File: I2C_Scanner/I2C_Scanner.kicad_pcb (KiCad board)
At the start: 4 copper layers, 63 x 30 mm, 59 parts, among them J1 USB_B_Micro, J2 Conn_01x02_Pin, J5 Conn_01x20_Pin, SW1 SW_Push, U1 RP2040, U2 NCP1117-3.3_SOT223, U3 W25Q128JVS, U4 NCP1117-1.8_SOT223, U5 TXS0108EPW, U6 TXS0108EPW, U7 TXS0108EPW, Y1 ABM8-272-T3

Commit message: v0.2
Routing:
- net +3.3V: track 32.7 -> 49.9 mm, vias 3 -> 5

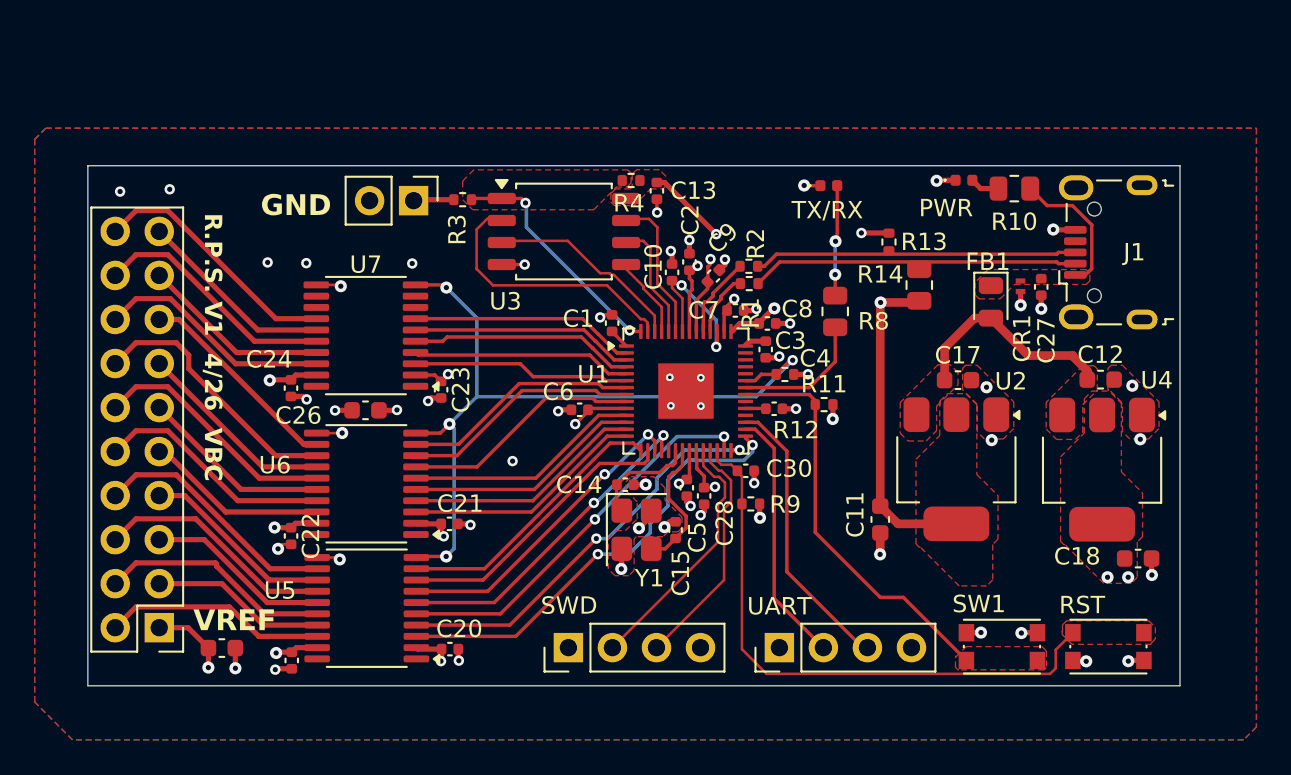
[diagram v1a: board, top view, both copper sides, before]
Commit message: Added USB C
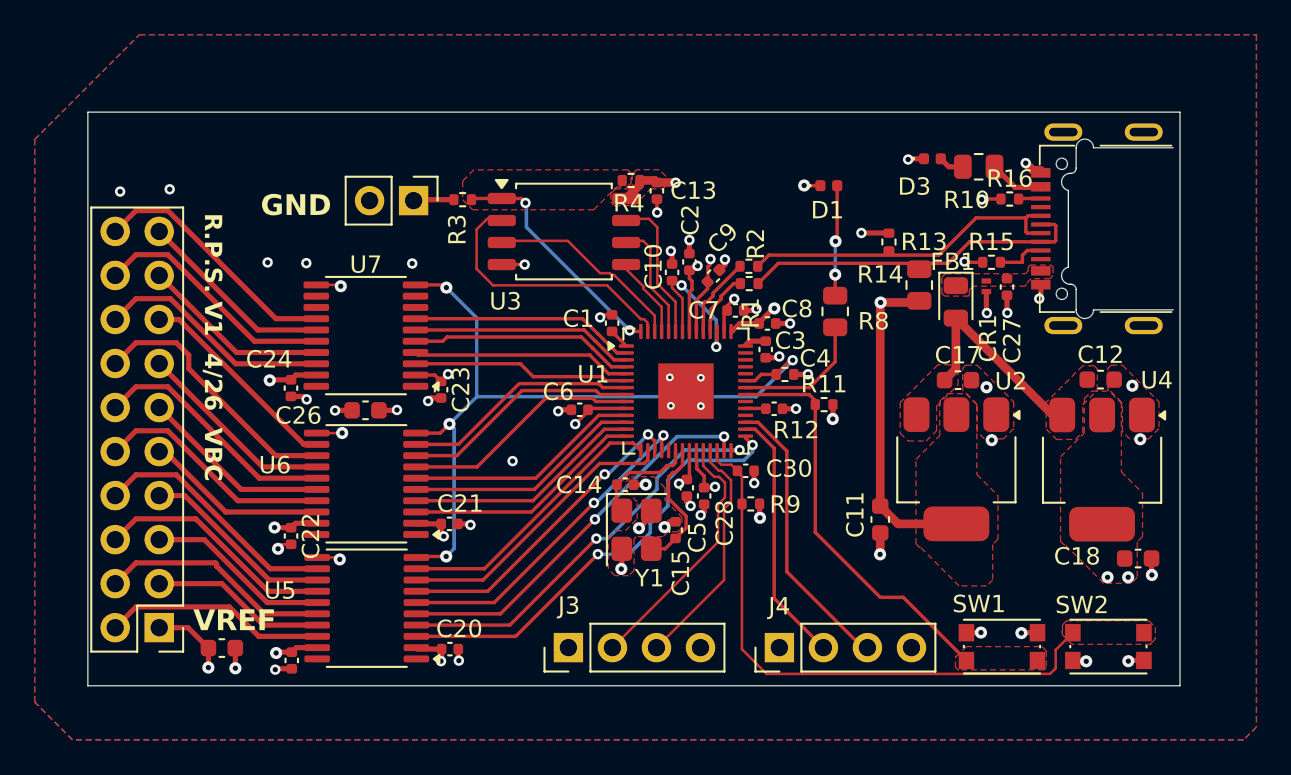
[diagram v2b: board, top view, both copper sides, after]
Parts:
- removed J1: USB_B_Micro, Connector_USB:USB_Micro-B_Wuerth_629105150521
- added J6: USB_C_Receptacle_USB2.0_14P, USB_C_Footprint:TYPE-C-31-M-14, F.Cu at (101.9, 45.6)
- added R15: 1.5KΩ, Resistor_SMD:R_0402_1005Metric, F.Cu at (94.1, 47.6)
- added R16: 1.5KΩ, Resistor_SMD:R_0402_1005Metric, F.Cu at (95.2, 43.9)
- moved R10 2.41 mm to (93.4, 42.1)
- moved D3 2.20 mm to (90.7, 41.6)
- moved FB1 2.02 mm to (92.1, 49.9)
- moved C27 1.98 mm to (95.0, 49.0)
- moved CR1 1.97 mm to (93.8, 49.0)
- renumbered TX/RX to D1, PWR to D3, SWD to J3, UART to J4, RST to SW2
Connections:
- C13 pad 1: +3.3V -> +1.8V
- R4 pad 2: +3.3V -> +1.8V
- U3 pad 8: +3.3V -> +1.8V
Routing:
- net +3.3V: track 49.9 -> 43.6 mm, vias 5 -> 4
- net /VBUS: track 8.05 -> 3.20 mm
- net +1.8V: track 24.8 -> 28.3 mm, vias 12 -> 13
- net GND: track 38.1 -> 41.5 mm, vias 55 -> 58
- net Net-(J6-CC1): track 0.00 -> 2.85 mm
- net Net-(J6-CC2): track 0.00 -> 1.29 mm
- net /USB_D-: track 18.9 -> 19.9 mm
- net /USB_D+: track 18.7 -> 19.2 mm
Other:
- board size 63 x 30 mm -> 63 x 33.1 mm

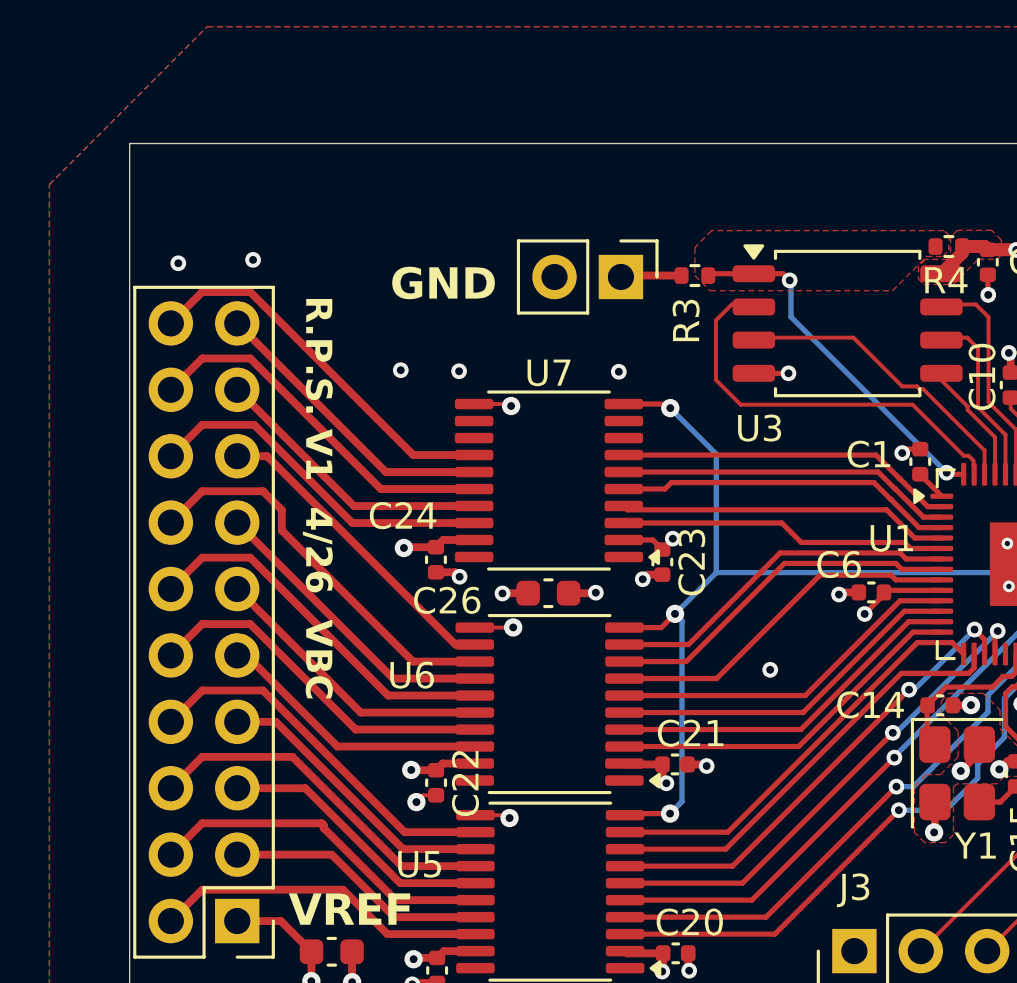
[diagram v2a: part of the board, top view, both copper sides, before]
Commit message: Added Contributer Name
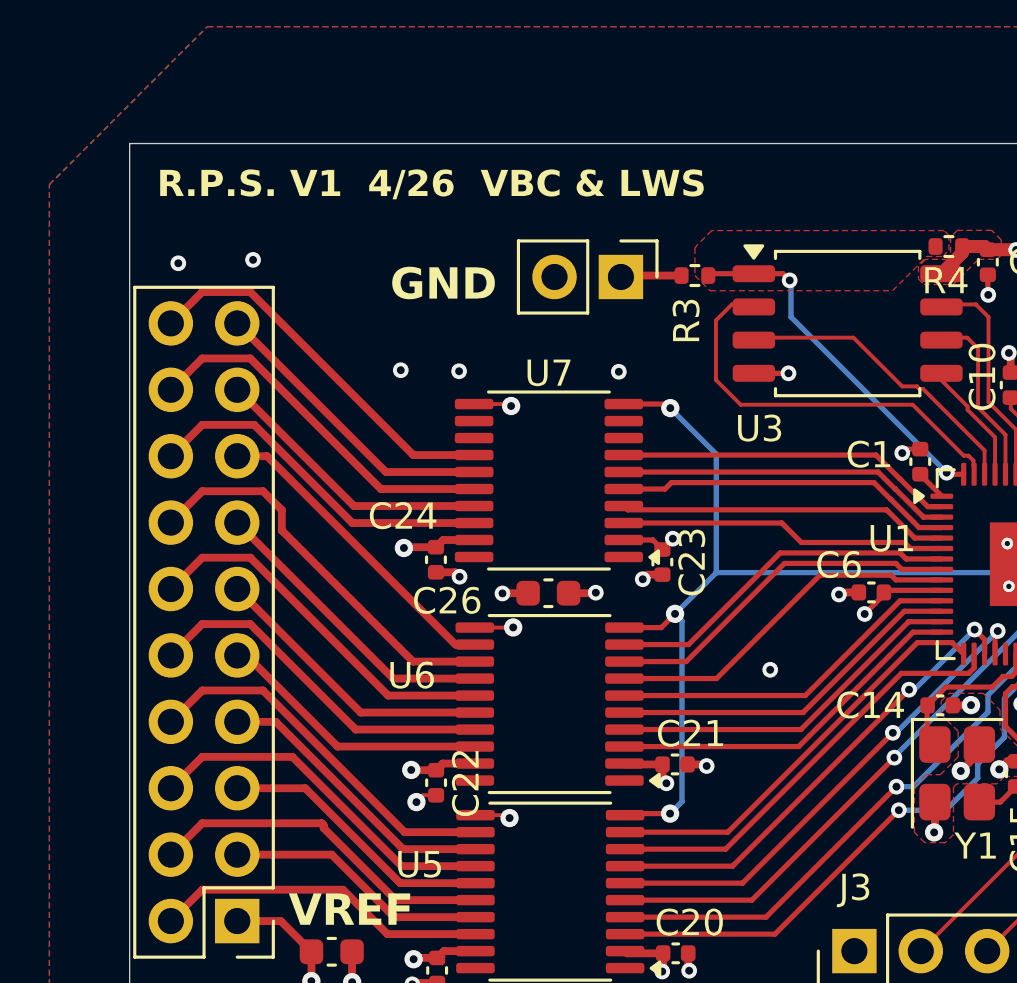
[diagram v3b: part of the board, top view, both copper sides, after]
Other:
- board text added: "R.P.S. V1 4/26 VBC & LWS"
- board text removed: "R.P.S. V1 4/26 VBC"
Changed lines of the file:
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@@
 		(layer "Edge.Cuts")
 	)
-	(gr_text "R.P.S. V1  4/26  VBC"
-		(at 48.63 44.73 270)
+	(gr_text "R.P.S. V1  4/26  VBC & LWS"
+		(at 43.04 41.04 0)
 		(layer "F.SilkS")
 		(effects
